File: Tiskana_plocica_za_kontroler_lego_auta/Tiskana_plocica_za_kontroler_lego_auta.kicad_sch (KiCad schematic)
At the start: 3 parts, among them J1 Conn_01x05, J2 Conn_01x20, J3 Conn_01x20

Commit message: kontroler fix
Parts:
- removed J1: Conn_01x05, Connector_PinHeader_2.54mm:PinHeader_1x05_P2.54mm_Vertical, symbol Connector_Generic:Conn_01x05
- added D1, D2, D3, D4: LED, LED_SMD:LED_0805_2012Metric, symbol Device:LED
- added J1, J5: Conn_01x02, Connector_JST:JST_PH_B2B-PH-K_1x02_P2.00mm_Vertical, symbol Connector_Generic:Conn_01x02
- added J4: Conn_01x05, Connector_PinSocket_2.54mm:PinSocket_1x05_P2.54mm_Vertical, symbol Connector_Generic:Conn_01x05
- added R1, R2, R3, R4: R, Resistor_SMD:R_0805_2012Metric, symbol Device:R
- added R5, R6: 100k, Resistor_SMD:R_0805_2012Metric, symbol Device:R
- added SW1: SW_SPST, Button_Switch_THT:SW_DIP_SPSTx01_Piano_10.8x4.1mm_W7.62mm_P2.54mm, symbol Switch:SW_SPST
- J3: footprint Connector_PinHeader_2.54mm:PinHeader_1x20_P2.54mm_Vertical -> Connector_PinSocket_2.54mm:PinSocket_1x20_P2.54mm_Vertical
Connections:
- net at J3.20 (Pin_20): now also D1.1 (K), D2.1 (K), D3.1 (K), D4.1 (K), J4.1 (Pin_1), R6.2
- net at J2.1 (Pin_1): now also J4.2 (Pin_2), SW1.1 (A)
- net at J2.10 (Pin_10): now also R2.1
- net at J2.11 (Pin_11): now also R3.1
- net at J2.14 (Pin_14): now also R4.1
- net at J2.2 (Pin_2): now also SW1.2 (B)
- net at J2.5 (Pin_5): now also J4.3 (Pin_3)
- net at J2.6 (Pin_6): now also J4.4 (Pin_4)
- net at J2.7 (Pin_7): now also J4.5 (Pin_5)
- net at J2.8 (Pin_8): now also R5.2, R6.1
- net at J2.9 (Pin_9): now also R1.1
- new net: D2.2 (A), R3.2
- new net: D3.2 (A), R2.2
- new net: D4.2 (A), R1.2
- new net: D1.2 (A), R4.2
- new net: J1.1 (Pin_1), J5.1 (Pin_1), R5.1
- new net: J1.2 (Pin_2), J5.2 (Pin_2)
- no-connect marks 35 -> 29
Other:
- note added: "EN"
- note added: "Kontroler za Lego Auto"
- note removed: "keyes + lolin32"
- moved on the sheet: J2, J3

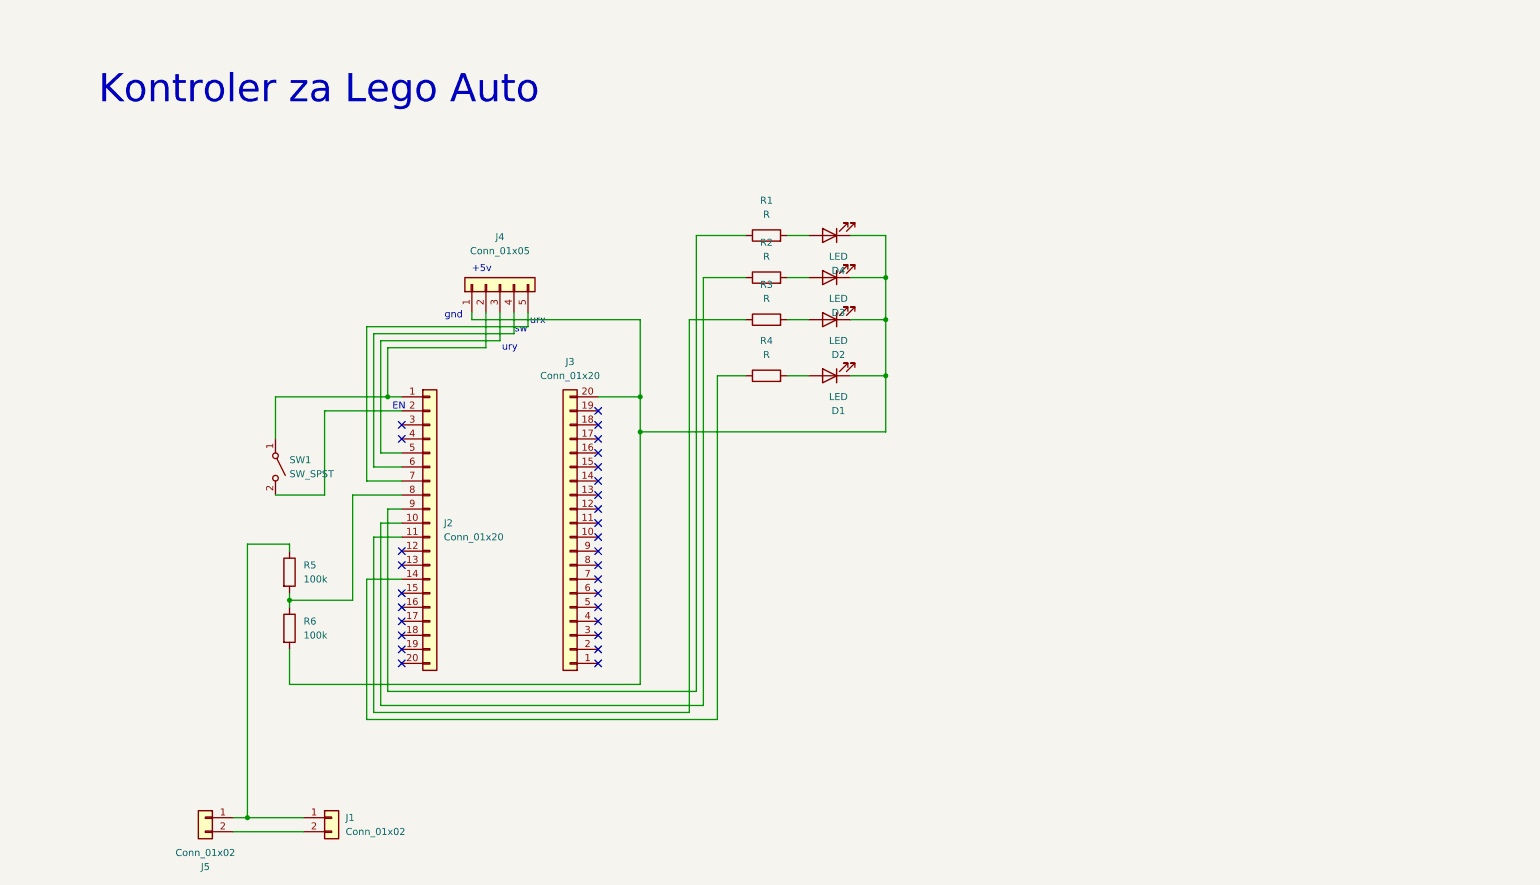
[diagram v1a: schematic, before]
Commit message: PCB kontroler
poboljsanje sheme i rad na pcbu
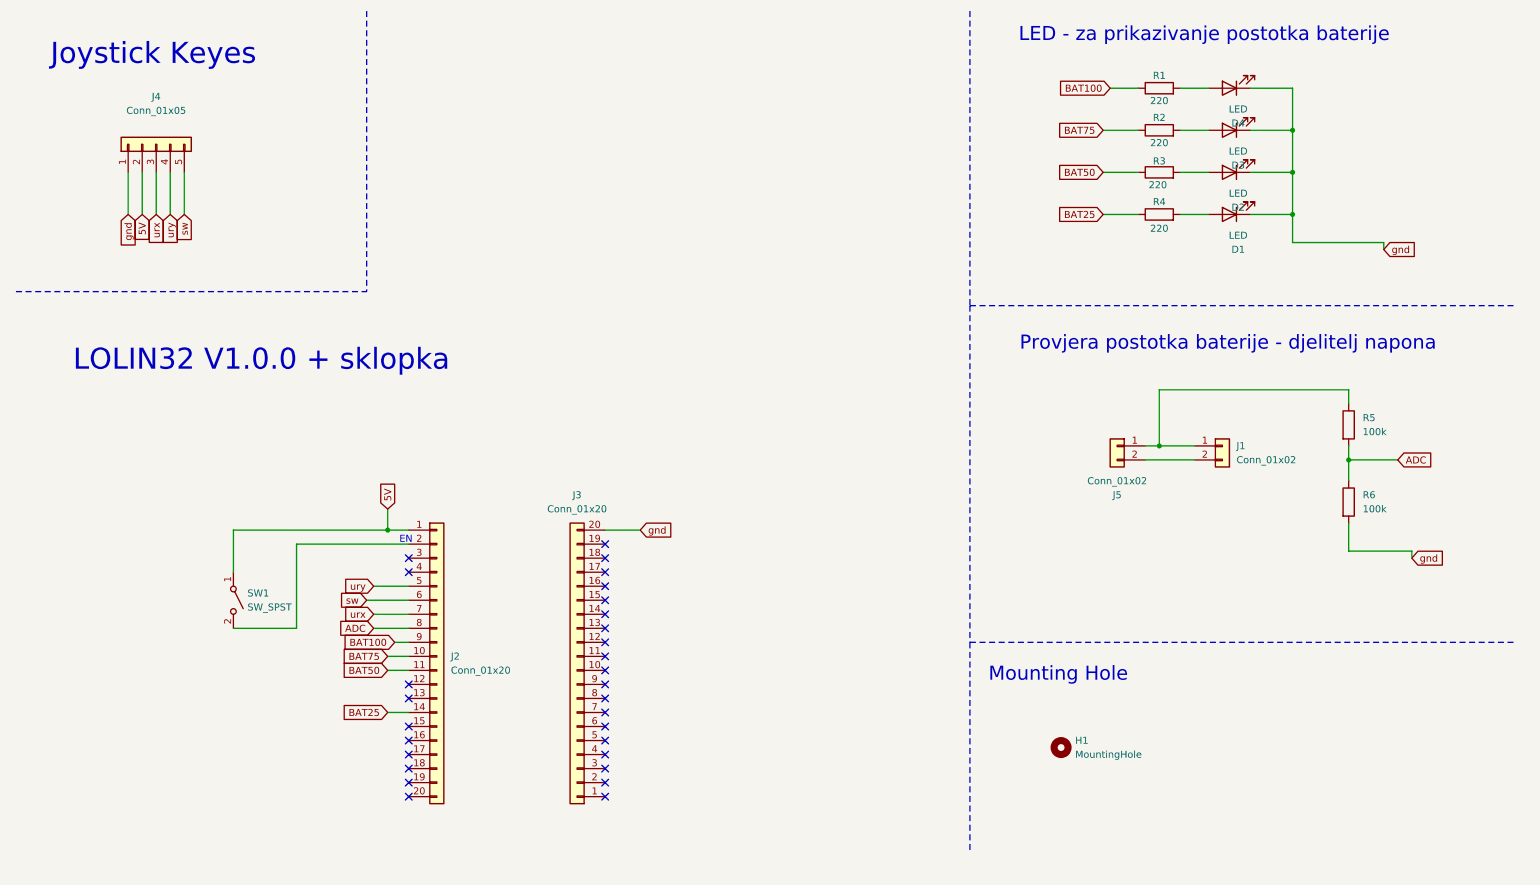
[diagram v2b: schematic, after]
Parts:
- added H1: MountingHole, MountingHole:MountingHole_5.3mm_M5, symbol Mechanical:MountingHole
- J2: footprint Connector_PinHeader_2.54mm:PinHeader_1x20_P2.54mm_Vertical -> Connector_PinSocket_2.54mm:PinSocket_1x20_P2.54mm_Vertical
- R1, R2, R3, R4: value R -> 220
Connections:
- net gnd: now reaches D1.1 (K), D2.1 (K), D3.1 (K), D4.1 (K), J3.20 (Pin_20), J4.1 (Pin_1), R6.2
- net BAT75: now reaches J2.10 (Pin_10), R2.1
- net BAT50: now reaches J2.11 (Pin_11), R3.1
- net 5V: now reaches J2.1 (Pin_1), J4.2 (Pin_2), SW1.1 (A)
- net urx: now reaches J4.3 (Pin_3)
- net urx: now also J2.7 (Pin_7); no longer J2.5 (Pin_5)
- net sw: now reaches J2.6 (Pin_6)
- net sw: now also J4.5 (Pin_5); no longer J4.4 (Pin_4)
- net BAT100: now reaches J2.9 (Pin_9), R1.1
- net BAT25: now reaches J2.14 (Pin_14), R4.1
- net ADC: now reaches J2.8 (Pin_8), R5.2, R6.1
- new net ury: J2.5 (Pin_5), J4.4 (Pin_4)
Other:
- note added: "Joystick Keyes"
- note added: "LED - za prikazivanje postotka baterije"
- note added: "LOLIN32 V1.0.0 + sklopka"
- note added: "Mounting Hole"
- note added: "Provjera postotka baterije - djelitelj napona"
- note removed: "+5v"
- note removed: "Kontroler za Lego Auto"
- note removed: "gnd"
- note removed: "sw"
- note removed: "urx"
- note removed: "ury"
- moved on the sheet: D1, D2, D3, D4, J1, J2, J3, J4, J5, R1, R2, R3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

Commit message: fix
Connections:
- net GND: now reaches J3.1 (Pin_1)
- net GND: now also D1.1 (K), D2.1 (K), D3.1 (K), D4.1 (K), J4.1 (Pin_1), R6.2
- net 5V renamed +5V
- removed net gnd: D1.1 (K), D2.1 (K), D3.1 (K), D4.1 (K), J3.20 (Pin_20), J4.1 (Pin_1), R6.2
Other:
- moved on the sheet: J3, J4

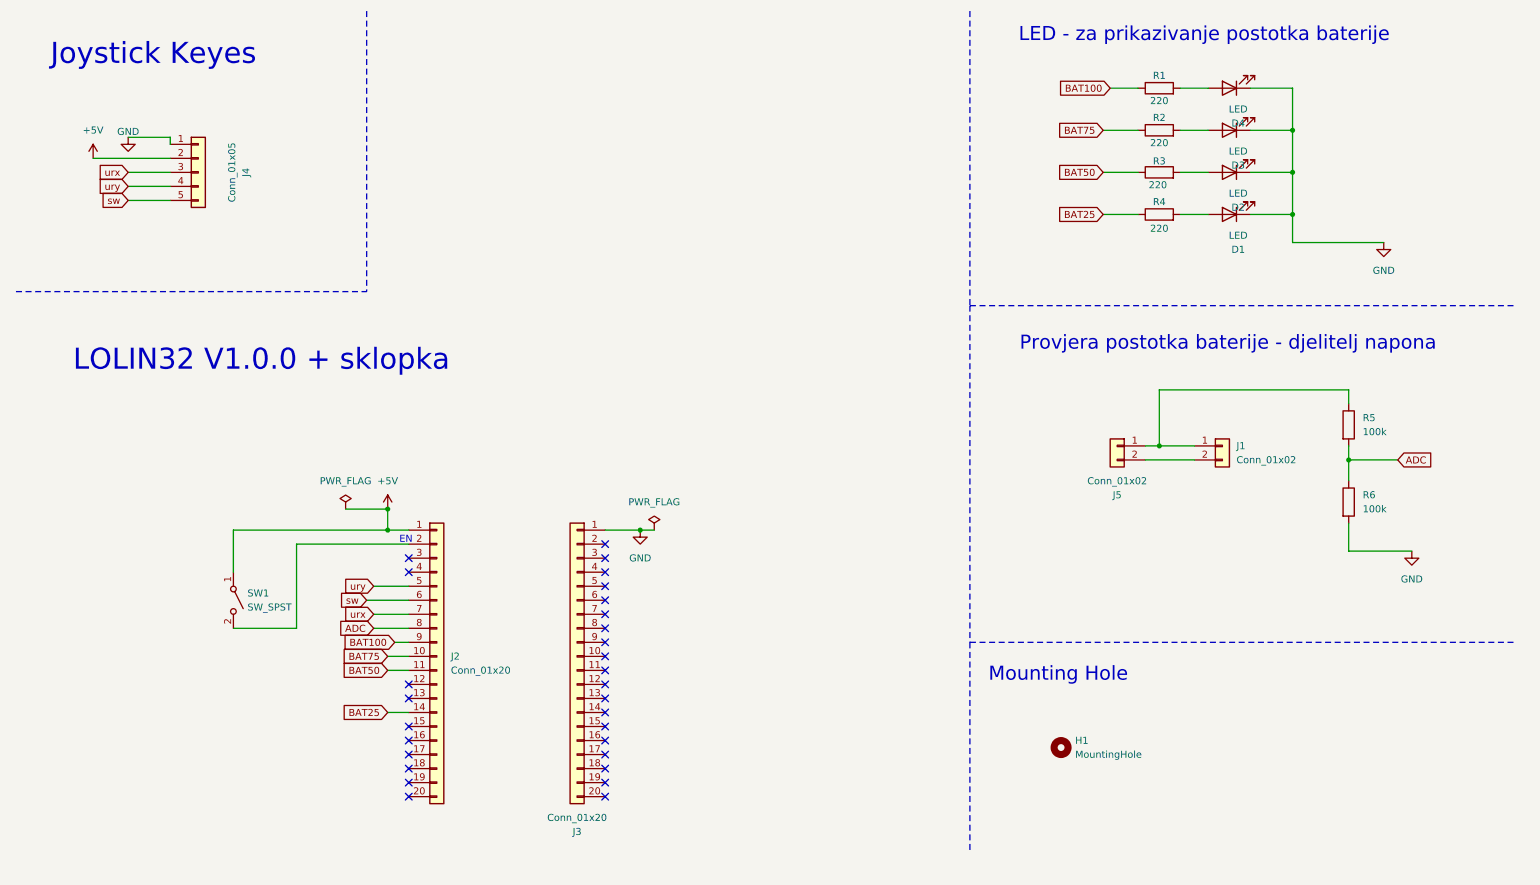
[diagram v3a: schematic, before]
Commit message: Kontroler pločica final
Popravak sheme pcb-a kod kontroler pločice
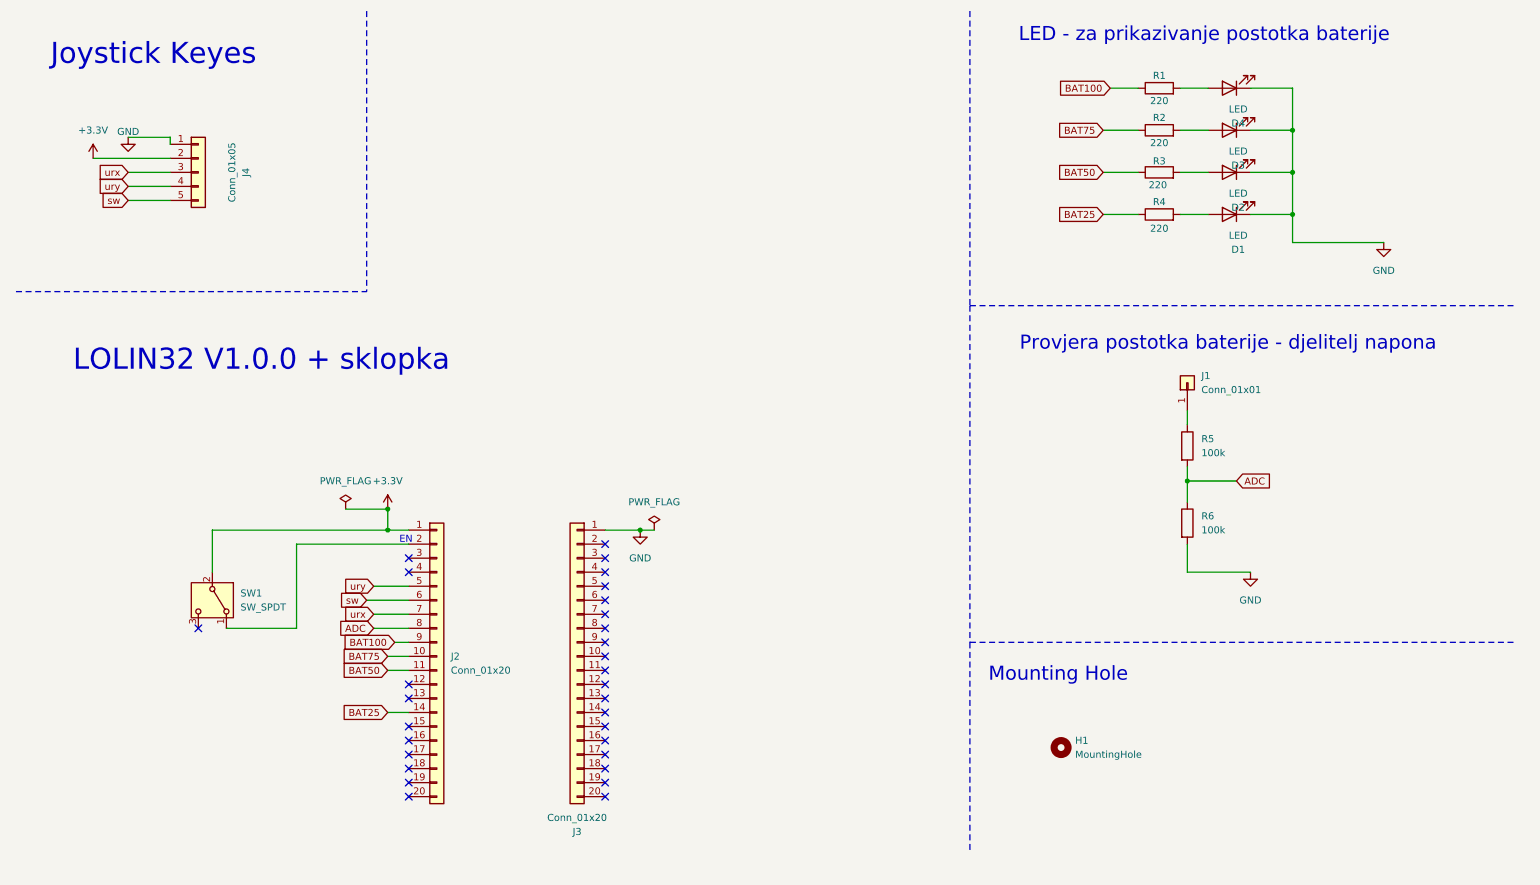
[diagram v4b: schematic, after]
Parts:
- removed J1, J5: Conn_01x02, Connector_JST:JST_PH_B2B-PH-K_1x02_P2.00mm_Vertical, symbol Connector_Generic:Conn_01x02
- removed SW1: SW_SPST, Button_Switch_THT:SW_DIP_SPSTx01_Piano_10.8x4.1mm_W7.62mm_P2.54mm, symbol Switch:SW_SPST
- added J1: Conn_01x01, Connector_PinSocket_2.54mm:PinSocket_1x01_P2.54mm_Vertical, symbol Connector_Generic:Conn_01x01
- added SW1: SW_SPDT, Button_Switch_THT:SW_Slide-03_Wuerth-WS-SLTV_10x2.5x6.4_P2.54mm, symbol Switch:SW_SPDT
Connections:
- net at J2.2 (Pin_2): now also SW1.1 (A)
- net at R5.1: now also J1.1 (Pin_1)
- net +5V renamed +3.3V
- net +3.3V: now also SW1.2 (B)
- no-connect marks 29 -> 30
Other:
- moved on the sheet: R5, R6
